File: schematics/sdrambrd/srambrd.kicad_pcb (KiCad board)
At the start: 2 copper layers, 33 x 83.8 mm, 13 parts, among them J1 LEFT, J2 Micro_SD_Card, J3 Conn_01x03, U1 IS61LV25616AL

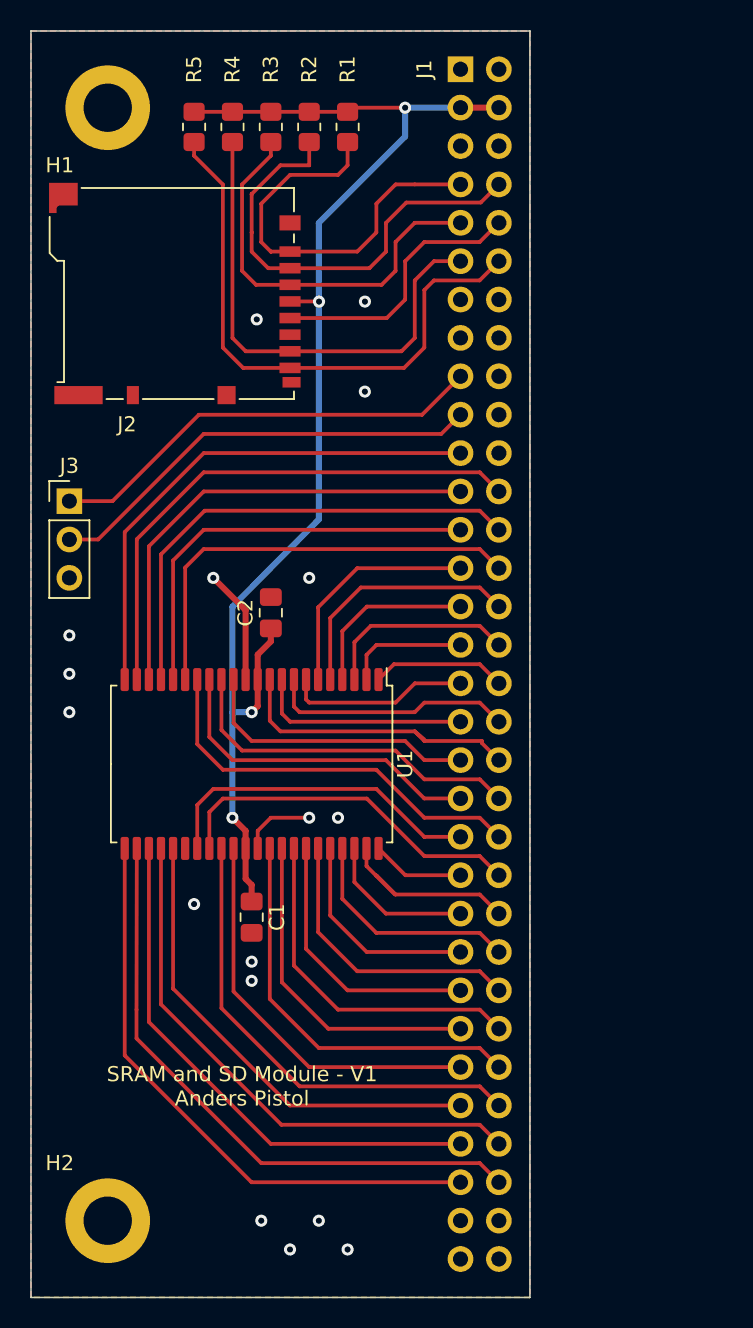
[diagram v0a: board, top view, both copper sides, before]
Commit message: Rv32: Updated SRAM brd schematic. Also updated legend in lcdbrd.
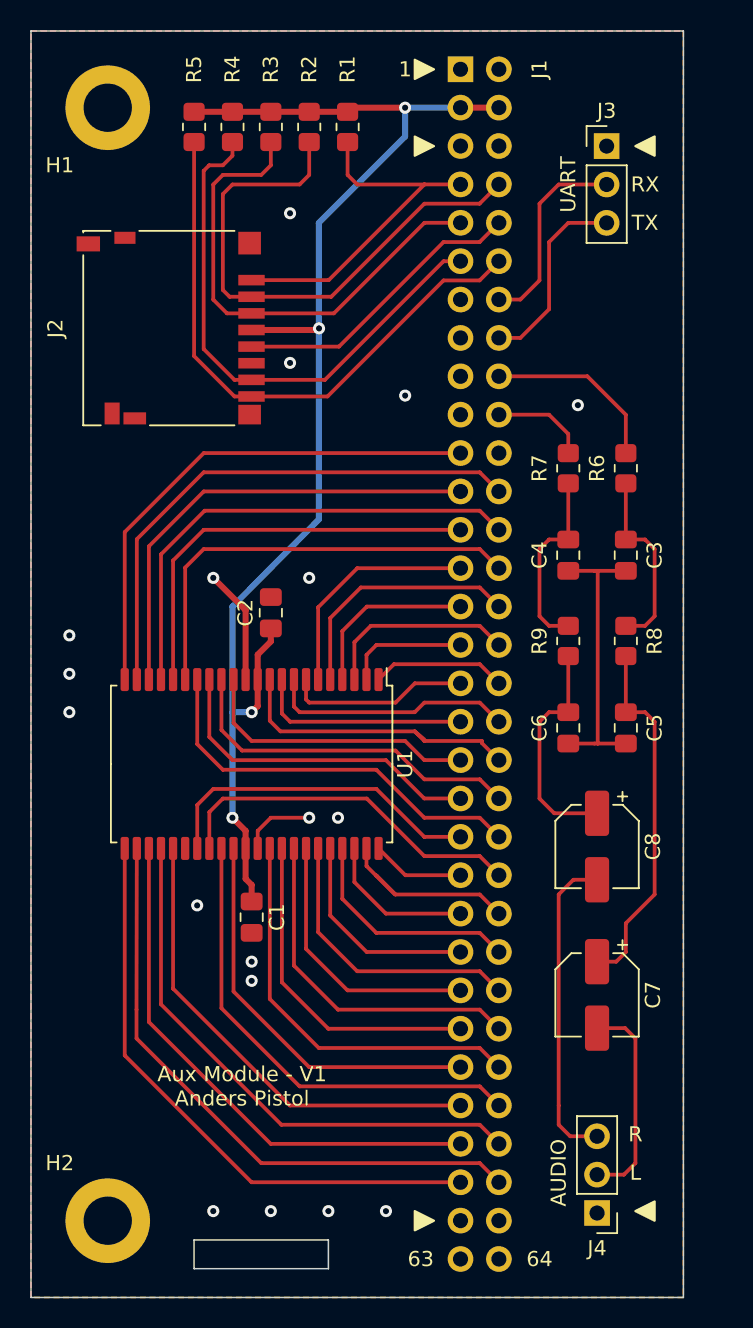
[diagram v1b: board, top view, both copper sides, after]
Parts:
- added C3: 10nF, Capacitor_SMD:C_0805_2012Metric_Pad1.18x1.45mm_HandSolder, F.Cu at (142.2, 94.4)
- added C4: 10nF, Capacitor_SMD:C_0805_2012Metric_Pad1.18x1.45mm_HandSolder, F.Cu at (138.4, 94.4)
- added C5: 10nF, Capacitor_SMD:C_0805_2012Metric_Pad1.18x1.45mm_HandSolder, F.Cu at (142.2, 105.8)
- added C6: 10nF, Capacitor_SMD:C_0805_2012Metric_Pad1.18x1.45mm_HandSolder, F.Cu at (138.4, 105.8)
- added C7: 100uF, Capacitor_SMD:CP_Elec_5x5.3, F.Cu at (140.3, 123.5)
- added C8: 100uF, Capacitor_SMD:CP_Elec_5x5.3, F.Cu at (140.3, 113.7)
- added J4: Conn_01x03, Connector_PinHeader_2.54mm:PinHeader_1x03_P2.54mm_Vertical, F.Cu at (140.3, 137.9)
- added R6: 4k7, Resistor_SMD:R_0805_2012Metric_Pad1.20x1.40mm_HandSolder, F.Cu at (142.2, 88.6)
- added R7: 4k7, Resistor_SMD:R_0805_2012Metric_Pad1.20x1.40mm_HandSolder, F.Cu at (138.4, 88.6)
- added R8: 4k7, Resistor_SMD:R_0805_2012Metric_Pad1.20x1.40mm_HandSolder, F.Cu at (142.2, 100.1)
- added R9: 4k7, Resistor_SMD:R_0805_2012Metric_Pad1.20x1.40mm_HandSolder, F.Cu at (138.4, 100.1)
- J2: footprint Connector_Card:microSD_HC_Hirose_DM3BT-DSF-PEJS -> Connector_Card:microSD_HC_Hirose_DM3D-SF
- moved J3 42.6 mm to (141.0, 67.3)
- moved J2 2.31 mm to (112.1, 79.4), turned to 90 degrees
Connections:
- J1 pad 14: unconnected-(J1-Pad14) -> RX
- J1 pad 16: unconnected-(J1-Pad16) -> TX
- J1 pad 17: RX -> unconnected-(J1-Pad17)
- J1 pad 18: unconnected-(J1-Pad18) -> PWM_L
- J1 pad 19: TX -> unconnected-(J1-Pad19)
- J1 pad 20: unconnected-(J1-Pad20) -> PWM_R
- J3 pad 1: RX -> GND
- J3 pad 2: TX -> RX
- J3 pad 3: GND -> TX
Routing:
- net Net-(C5-Pad1): track 0.00 -> 24.1 mm
- net AUDIO_R: track 0.00 -> 21.0 mm
- net Net-(C3-Pad2): track 0.00 -> 19.0 mm
- net TX: track 29.3 -> 12.9 mm
- net RX: track 29.3 -> 13.3 mm
- net Net-(C6-Pad2): track 0.00 -> 15.2 mm
- net AUDIO_L: track 0.00 -> 13.9 mm
- net Net-(C4-Pad2): track 0.00 -> 12.5 mm
- net Net-(C3-Pad1): track 0.00 -> 12.5 mm
- net PWM_L: track 0.00 -> 12.0 mm
- net PWM_R: track 0.00 -> 6.39 mm
- net SD_DAT3: track 30.2 -> 36.3 mm
- net SD_CMD: track 27.0 -> 32.7 mm
- net SD_DAT2: track 27.3 -> 24.0 mm
- net SD_DAT0: track 33.1 -> 36.1 mm
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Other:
- board size 33 x 83.8 mm -> 43.2 x 83.8 mm
- board text added: "1"
- board text added: "63"
- board text added: "64"
- board text added: "AUDIO"
- board text added: "Aux Module - V1 Anders Pistol"
- board text added: "L"
- board text added: "R"
- board text added: "RX"
- board text added: "TX"
- board text added: "UART"
- board text removed: "SRAM and SD Module - V1 Anders Pistol"

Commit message: Rv32: SRAM Aux board schematics updated. JLCPCB v1
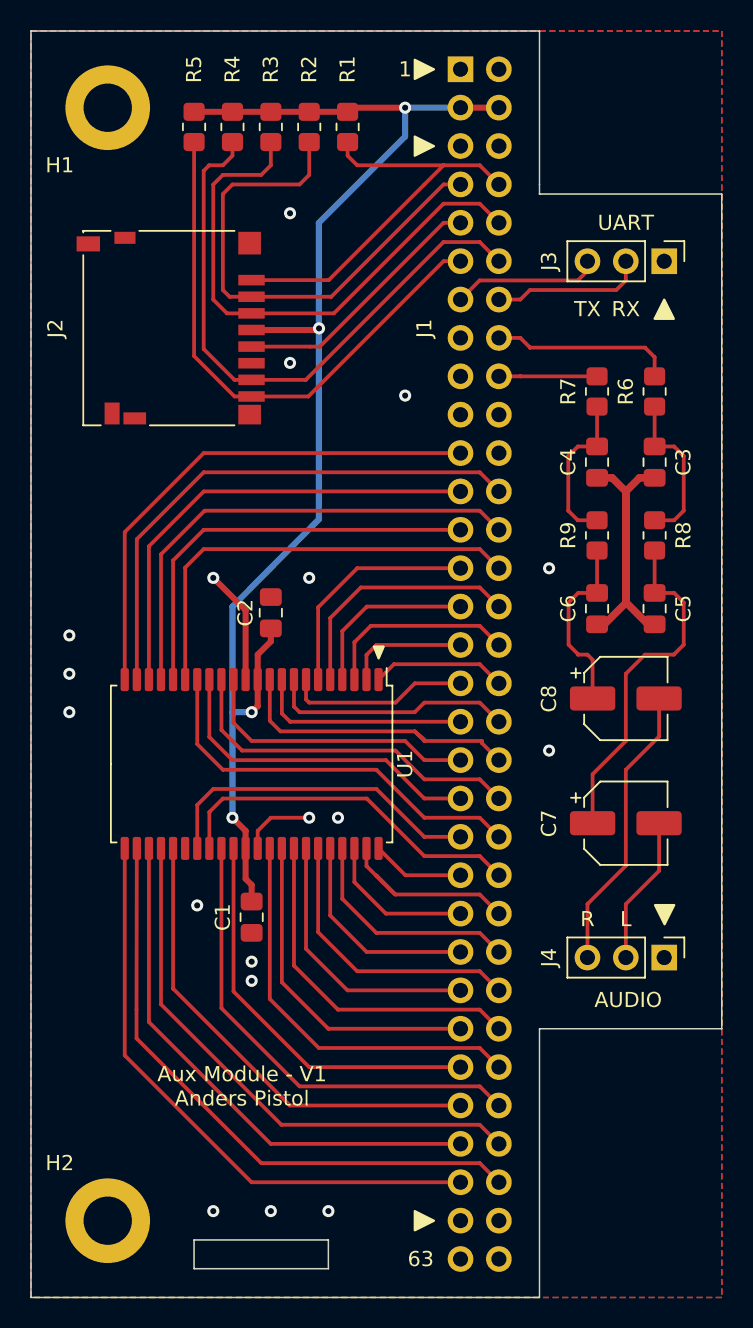
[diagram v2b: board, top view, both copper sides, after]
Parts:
- moved J4 17.5 mm to (144.8, 121.0), turned to -90 degrees
- moved C7 11.5 mm to (142.2, 112.1), turned to 0 degrees
- moved C8 9.98 mm to (142.2, 103.9), turned to 0 degrees
- moved J3 8.52 mm to (144.8, 74.9), turned to -90 degrees
- moved C5 8.12 mm to (144.1, 97.9)
- moved C6 8.12 mm to (140.3, 97.9)
- moved R8 7.24 mm to (144.1, 93.1)
- moved R9 7.24 mm to (140.3, 93.1)
- moved C3 6.44 mm to (144.1, 88.2)
- moved C4 6.44 mm to (140.3, 88.2)
- moved R6 5.43 mm to (144.1, 83.5)
- moved R7 5.43 mm to (140.3, 83.5)
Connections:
- J1 pad 10: SD_CLK -> SD_CMD
- J1 pad 11: SD_DAT0 -> SD_DAT1
- J1 pad 12: SD_DAT1 -> SD_DAT0
- J1 pad 13: unconnected-(J1-Pad13) -> TX
- J1 pad 16: TX -> PWM_L
- J1 pad 18: PWM_L -> PWM_R
- J1 pad 20: PWM_R -> unconnected-(J1-Pad20)
- J1 pad 7: SD_DAT2 -> SD_DAT3
- J1 pad 8: SD_DAT3 -> SD_DAT2
- J1 pad 9: SD_CMD -> SD_CLK
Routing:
- net Net-(C3-Pad2): track 19.0 -> 24.3 mm
- net AUDIO_L: track 13.9 -> 9.80 mm
- net SD_DAT0: track 36.1 -> 39.7 mm
- net SD_CMD: track 32.7 -> 36.3 mm
- net SD_DAT2: track 24.0 -> 27.6 mm
- net TX: track 12.9 -> 9.82 mm
- net RX: track 13.3 -> 10.2 mm
- net Net-(C6-Pad2): track 15.2 -> 12.3 mm
- net SD_DAT3: track 36.3 -> 33.8 mm
- net SD_DAT1: track 39.2 -> 36.6 mm
- net SD_CLK: track 19.8 -> 17.2 mm
- net AUDIO_R: track 21.0 -> 19.1 mm
- net Net-(C4-Pad2): track 12.5 -> 10.6 mm
- net Net-(C3-Pad1): track 12.5 -> 10.6 mm
- net Net-(C5-Pad1): track 24.1 -> 23.2 mm
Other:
- board size 43.2 x 83.8 mm -> 45.7 x 83.8 mm
- board text removed: "64"

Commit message: Rv32: Another revision of the AUX board, ordered from JLCPCB.
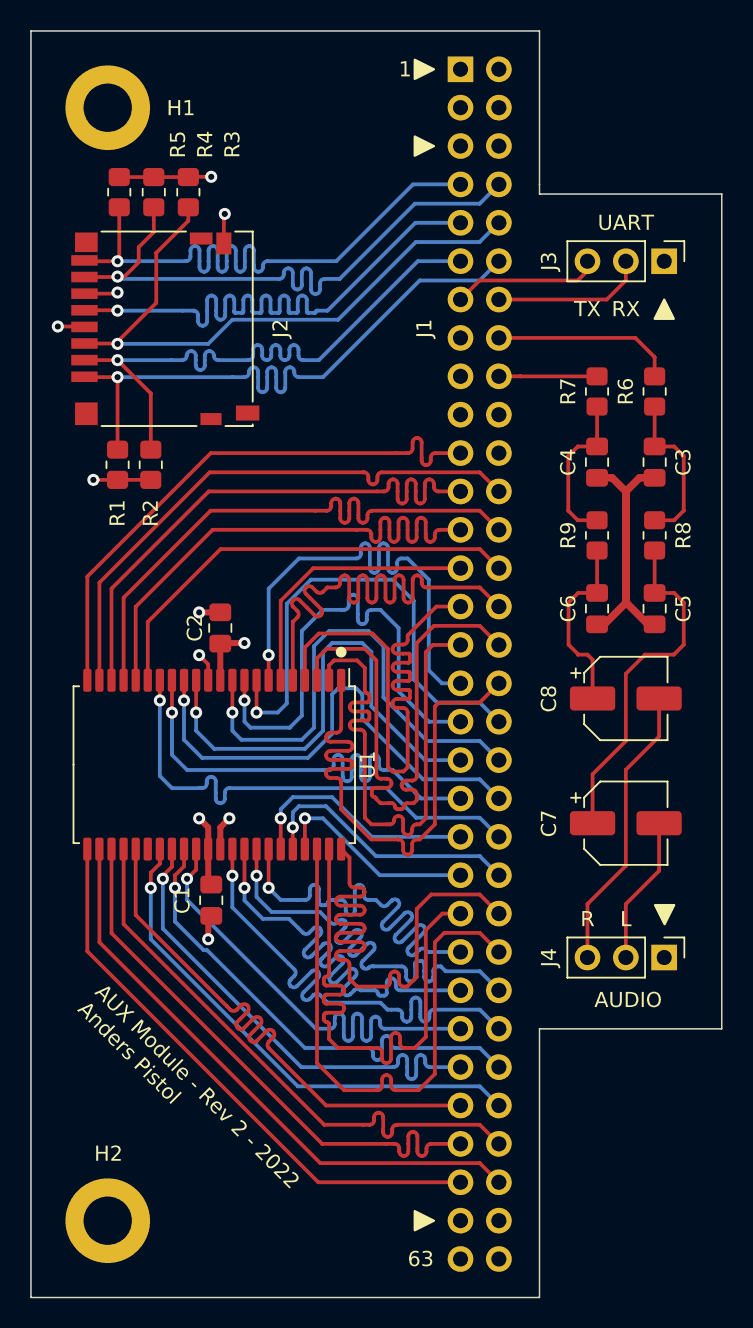
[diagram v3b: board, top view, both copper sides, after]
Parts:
- moved R1 27.1 mm to (108.6, 88.4), turned to 90 degrees
- moved R2 24.7 mm to (110.8, 88.4), turned to 90 degrees
- moved R3 6.96 mm to (113.3, 70.4)
- moved R4 6.76 mm to (111.0, 70.4)
- moved R5 6.57 mm to (108.7, 70.4)
- moved C2 3.49 mm to (115.4, 99.2)
- moved C1 2.90 mm to (114.8, 117.2)
- moved U1 2.48 mm to (115.0, 108.2)
- moved J2 0.36 mm to (111.8, 79.4), turned to -90 degrees
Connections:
- J1 pad 11: SD_DAT1 -> SD_DAT3
- J1 pad 12: SD_DAT0 -> SD_DAT2
- J1 pad 41: D8 -> LB_N
- J1 pad 43: A17 -> OE_N
- J1 pad 44: D9 -> UB_N
- J1 pad 45: A15 -> A16
- J1 pad 46: A16 -> A17
- J1 pad 47: UB_N -> D15
- J1 pad 48: OE_N -> A15
- J1 pad 49: D15 -> D13
- J1 pad 50: LB_N -> D14
- J1 pad 51: D13 -> D11
- J1 pad 52: D14 -> D12
- J1 pad 53: D11 -> D9
- J1 pad 54: D12 -> D10
- J1 pad 56: D10 -> D8
- J1 pad 7: SD_DAT3 -> SD_DAT1
- J1 pad 8: SD_DAT2 -> SD_DAT0
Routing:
- net 3v3: track 90.1 -> 20.4 mm, vias 4 -> 5
- net A17: track 6.16 -> 38.7 mm
- net A1: track 8.13 -> 37.3 mm
- net A0: track 8.91 -> 37.4 mm
- net A15: track 10.1 -> 38.3 mm
- net A3: track 11.7 -> 38.1 mm
- net A2: track 13.0 -> 38.7 mm
- net A16: track 13.0 -> 37.4 mm
- net SD_CLK: track 17.2 -> 41.2 mm, vias 0 -> 1
- net D0: track 12.2 -> 32.9 mm, vias 0 -> 1
- net A4: track 16.6 -> 37.0 mm
- net D2: track 14.3 -> 32.3 mm, vias 0 -> 1
- net D1: track 16.3 -> 32.6 mm, vias 0 -> 1
- net D15: track 18.0 -> 32.2 mm, vias 0 -> 1
- net SD_DAT2: track 27.6 -> 41.6 mm, vias 0 -> 1
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- added copper zone on In2.Cu, net 3v3
- added copper zone on In1.Cu, net GND
- removed copper zone on B.Cu, net GND
- removed copper zone on F.Cu, net GND
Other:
- outline, holes or cut-outs redrawn
- copper layers 2 -> 4
- board text added: "AUX Module - Rev 2 - 2022 Anders Pistol"
- board text removed: "Aux Module - V1 Anders Pistol"
